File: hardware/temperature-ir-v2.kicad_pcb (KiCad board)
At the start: 2 copper layers, 20 x 25 mm, 24 parts, among them P1 CON-SENSOR2, P2 DEBUG, P3 BOOT, U1 XMC110024, U2 MLX90614, U4 DRILL, U5 DRILL, U6 DRILL, U7 DRILL

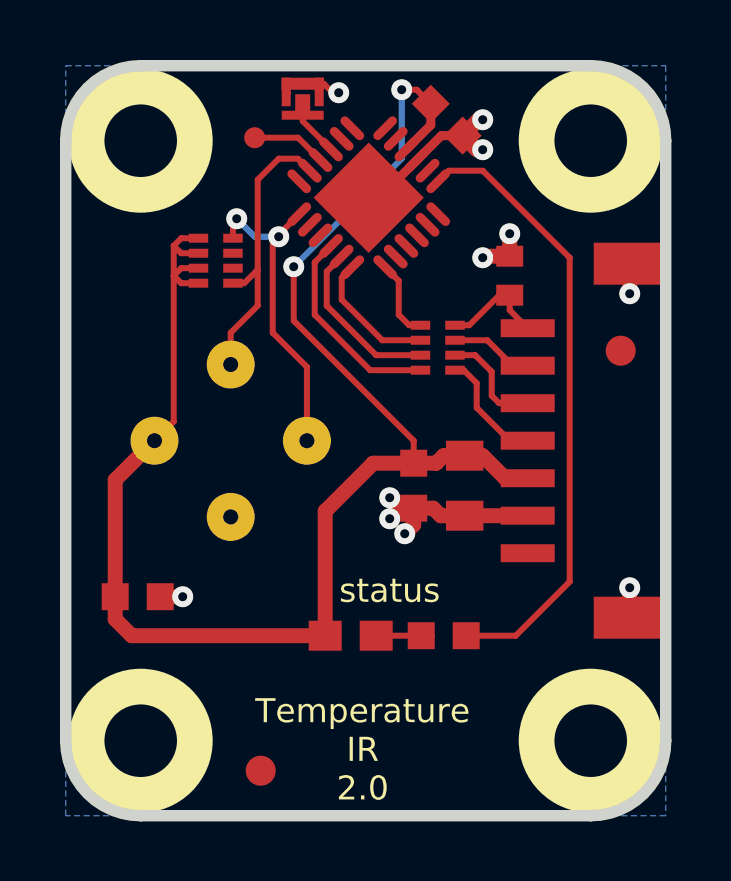
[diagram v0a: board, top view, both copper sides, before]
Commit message: Change capacitor footprint(s) to C0402F
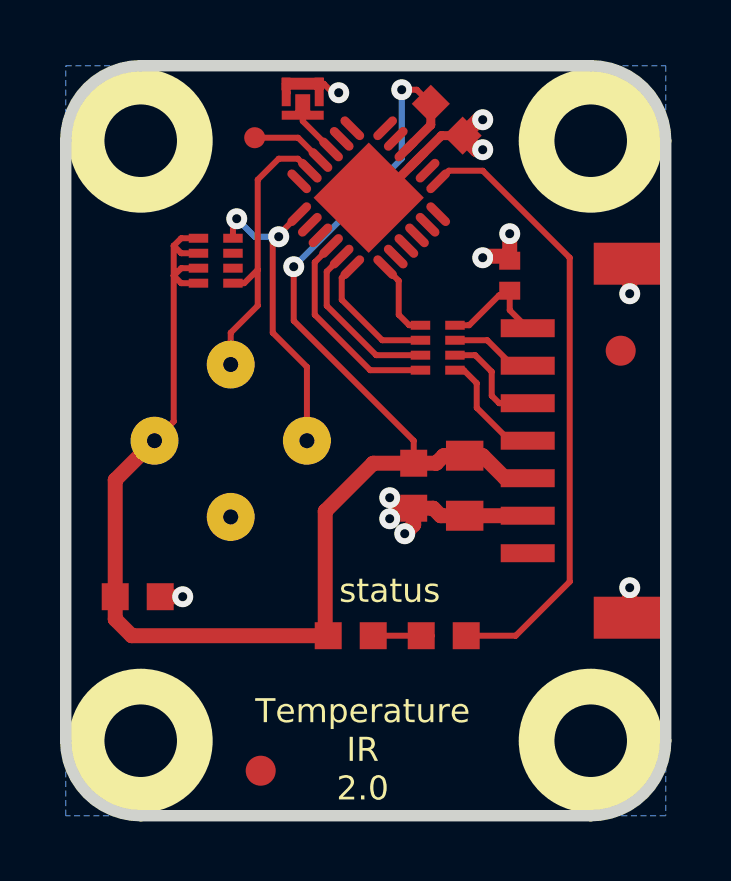
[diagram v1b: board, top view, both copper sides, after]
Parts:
- C2: footprint kicad-libraries:C0402E -> kicad-libraries:C0402F
- D1: footprint kicad-libraries:D0603E -> kicad-libraries:D0603F
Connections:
- P1 pad 1: (no net) -> +5V
- RP2 pad 6: (no net) -> Net-(RP2-Pad6)
- RP2 pad 7: (no net) -> Net-(RP2-Pad7)
- U1 pad 11: (no net) -> Net-(U1-Pad11)
- U1 pad 12: (no net) -> Net-(U1-Pad12)
- U1 pad 13: (no net) -> Net-(U1-Pad13)
- U1 pad 14: (no net) -> Net-(U1-Pad14)
- U1 pad 18: (no net) -> Net-(U1-Pad18)
- U1 pad 2: (no net) -> Net-(U1-Pad2)
- U1 pad 20: (no net) -> Net-(U1-Pad20)
- U1 pad 21: (no net) -> Net-(U1-Pad21)
- U1 pad 3: (no net) -> Net-(U1-Pad3)
- U1 pad 4: (no net) -> Net-(U1-Pad4)
- U1 pad 5: (no net) -> Net-(U1-Pad5)
- U1 pad 6: (no net) -> Net-(U1-Pad6)
- U1 pad 8: (no net) -> Net-(U1-Pad8)
